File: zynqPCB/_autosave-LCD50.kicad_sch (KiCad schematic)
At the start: 29 parts, among them J4 HDMI_A, Q2 IRLML2502, Q3 IRLML2502, Q4 IRLML2502, U19 PCA9306, U20B1 xc7z020clg484, U20D1 xc7z020clg484, U20E1 xc7z020clg484

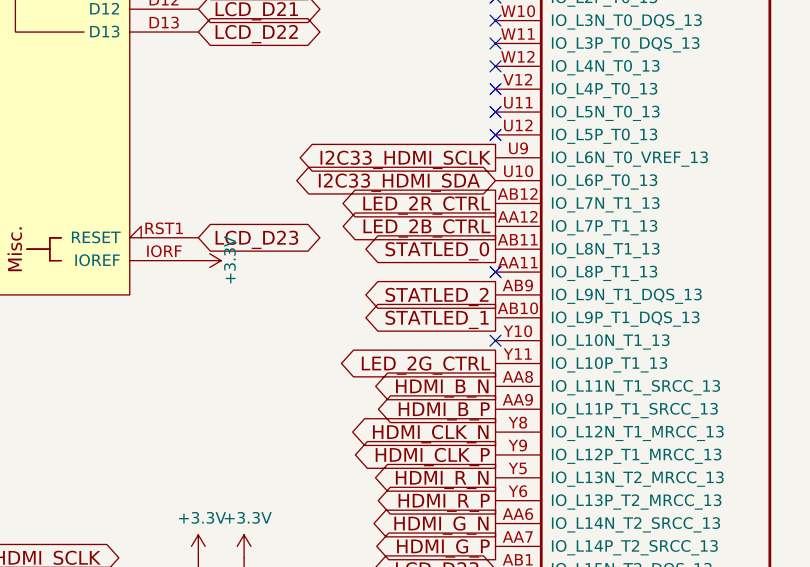
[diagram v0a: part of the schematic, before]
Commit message: removed grounded resistor can configure from the vivado and removed LCD
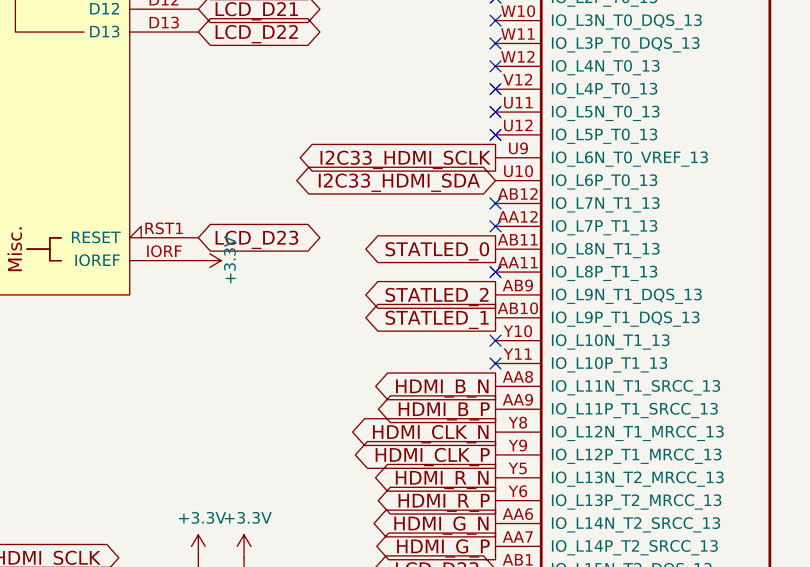
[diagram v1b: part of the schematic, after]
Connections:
- net LED_2B_CTRL: no longer names the net of U20B1.AA12 (IO_L7P_T1_13)
- net LED_2G_CTRL: no longer names the net of U20B1.Y11 (IO_L10P_T1_13)
- net LED_2R_CTRL: no longer names the net of U20B1.AB12 (IO_L7N_T1_13)
- no-connect marks 23 -> 26
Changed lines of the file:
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@@
+	)
+	(no_connect
+		(at 163.83 82.55)
 	)
 	(no_connect
@@
 	)
 	(no_connect
+		(at 163.83 80.01)
+	)
+	(no_connect
 		(at 163.83 44.45)
 	)
@@
 	(no_connect
 		(at 163.83 46.99)
+	)
+	(no_connect
+		(at 163.83 97.79)
 	)
 	(no_connect
@@
 		)
 	)
-	(global_label "LED_2R_CTRL"
-		(shape output)
-		(at 163.83 80.01 180)
-		(effects
-			(font
-				(size 1.524 1.524)
-			)
-			(justify right)
-		)
-		(property "Intersheetrefs" "${INTERSHEET_REFS}"
-			(at 163.83 80.01 0)
-			(effects
-				(font
-					(size 1.27 1.27)
-				)
-				(hide yes)
-			)
-		)
-	)
 	(global_label "I2C33_HDMI_SDA"
 		(shape bidirectional)
@@
 		)
 	)
-	(global_label "LED_2G_CTRL"
-		(shape output)
-		(at 163.83 97.79 180)
-		(effects
-			(font
-				(size 1.524 1.524)
-			)
-			(justify right)
-		)
-		(property "Intersheetrefs" "${INTERSHEET_REFS}"
-			(at 163.83 97.79 0)
-			(effects
-				(font
-					(size 1.27 1.27)
-				)
-				(hide yes)
-			)
-		)
-	)
 	(global_label "I2C5_HDMI_SCLK"
 		(shape input)
@@
 			(effects
 				(font
-					(size 1.27 1.27)
-				)
-				(hide yes)
-			)
-		)
-	)
-	(global_label "LED_2B_CTRL"
-		(shape output)
-		(at 163.83 82.55 180)
-		(effects
-			(font
-				(size 1.524 1.524)
-			)
-			(justify right)
-		)
-		(property "Intersheetrefs" "${INTERSHEET_REFS}"
-			(at 163.83 82.55 0)
-			(effects
-				(font

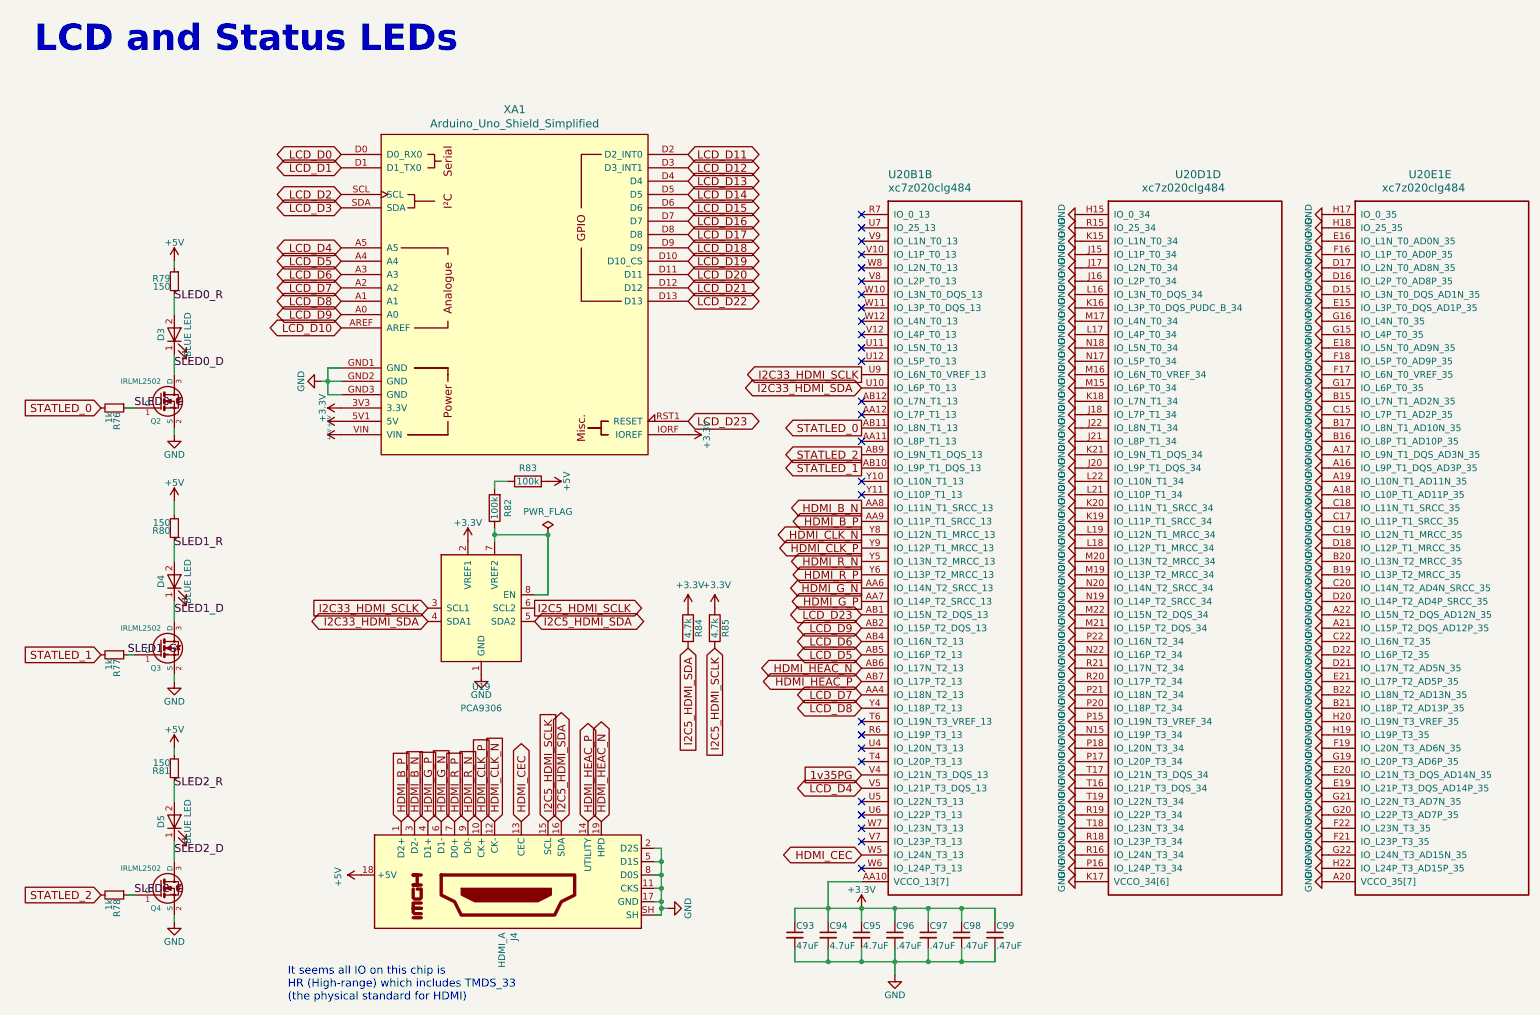
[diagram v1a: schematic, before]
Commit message: removed grounded resistor can configure from the vivado and removed LCD
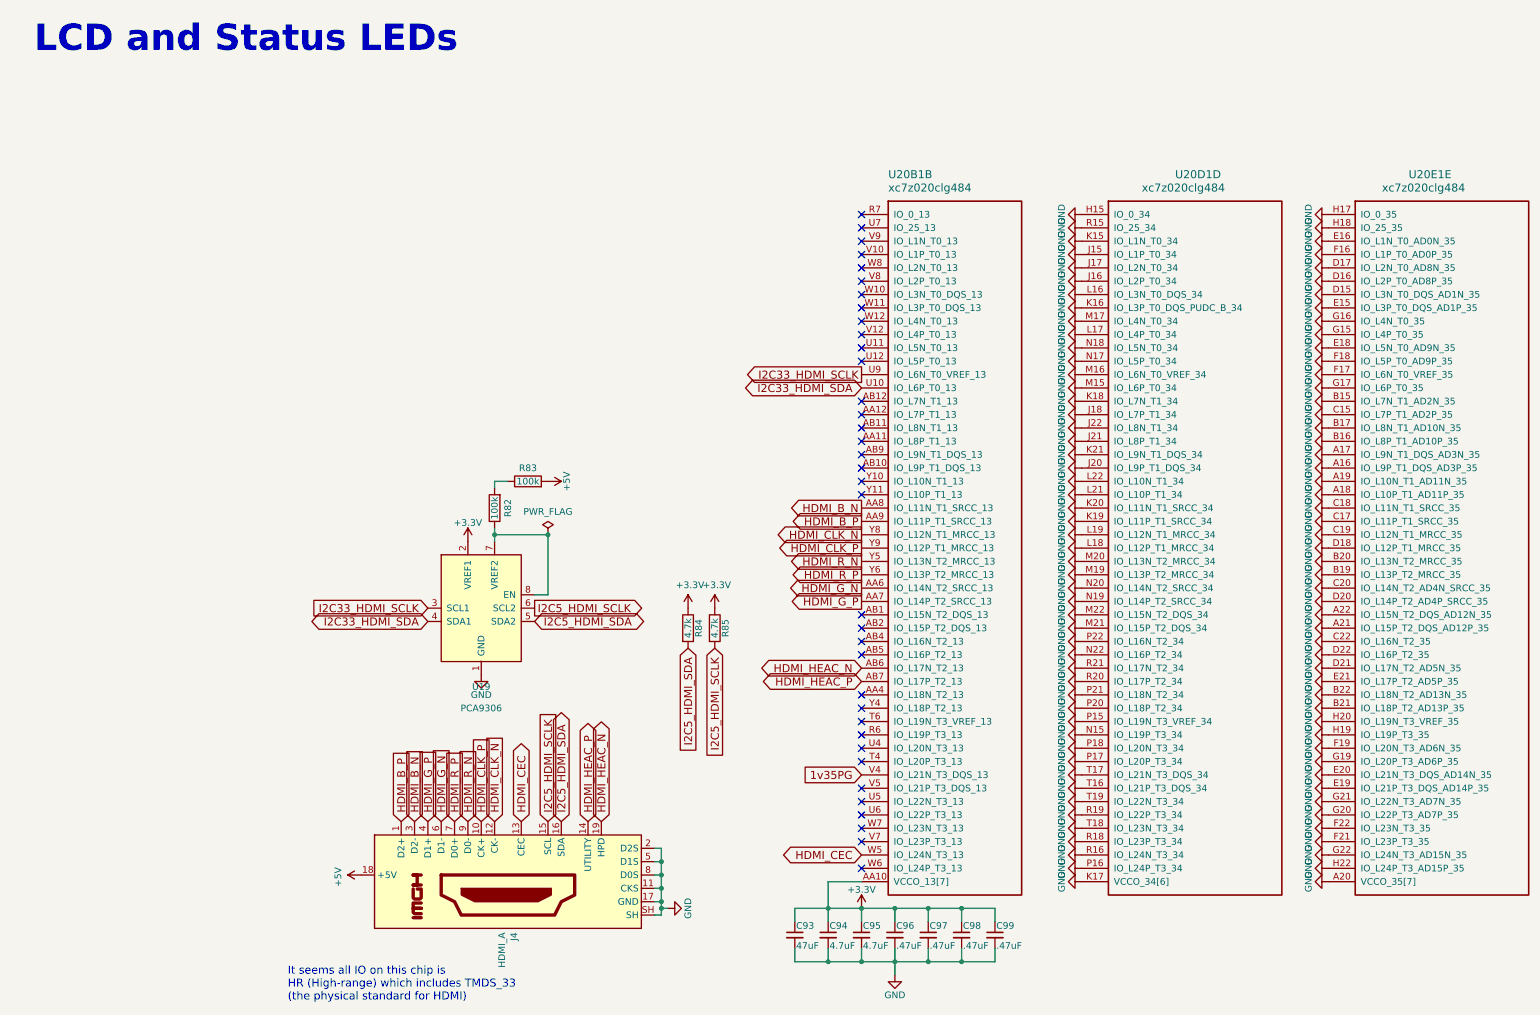
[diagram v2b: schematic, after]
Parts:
- removed D3, D4, D5: BLUE LED, Capacitor_SMD:C_0603_1608Metric, symbol DFTBoard-rescue:LED-
- removed Q2, Q3, Q4: IRLML2502, Package_TO_SOT_SMD:SOT-23, symbol DFTBoard-rescue:IRLML2502-
- removed R76, R77, R78: 1k, Resistor_SMD:R_0402_1005Metric, symbol Device:R_Small
- removed R79, R80, R81: 150, Resistor_SMD:R_0402_1005Metric, symbol Device:R_Small
- removed XA1: Arduino_Uno_Shield_Simplified, DFTcustom:Arduino_Uno_Shield_Simplified, symbol arduino:Arduino_Uno_Shield_Simplified
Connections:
- net LCD_D23: no longer names the net of U20B1.AB1 (IO_L15N_T2_DQS_13)
- net LCD_D4: no longer names the net of U20B1.V5 (IO_L21P_T3_DQS_13)
- net LCD_D5: no longer names the net of U20B1.AB5 (IO_L16P_T2_13)
- net LCD_D6: no longer names the net of U20B1.AB4 (IO_L16N_T2_13)
- net LCD_D7: no longer names the net of U20B1.AA4 (IO_L18N_T2_13)
- net LCD_D8: no longer names the net of U20B1.Y4 (IO_L18P_T2_13)
- net LCD_D9: no longer names the net of U20B1.AB2 (IO_L15P_T2_DQS_13)
- net STATLED_0: no longer names the net of U20B1.AB11 (IO_L8N_T1_13)
- net STATLED_1: no longer names the net of U20B1.AB10 (IO_L9P_T1_DQS_13)
- net STATLED_2: no longer names the net of U20B1.AB9 (IO_L9N_T1_DQS_13)
- no-connect marks 26 -> 36
